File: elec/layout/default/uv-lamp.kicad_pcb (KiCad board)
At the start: 2 copper layers, 21 x 21 mm, 3 parts, among them U1 ?, U2 ?, U3 ?

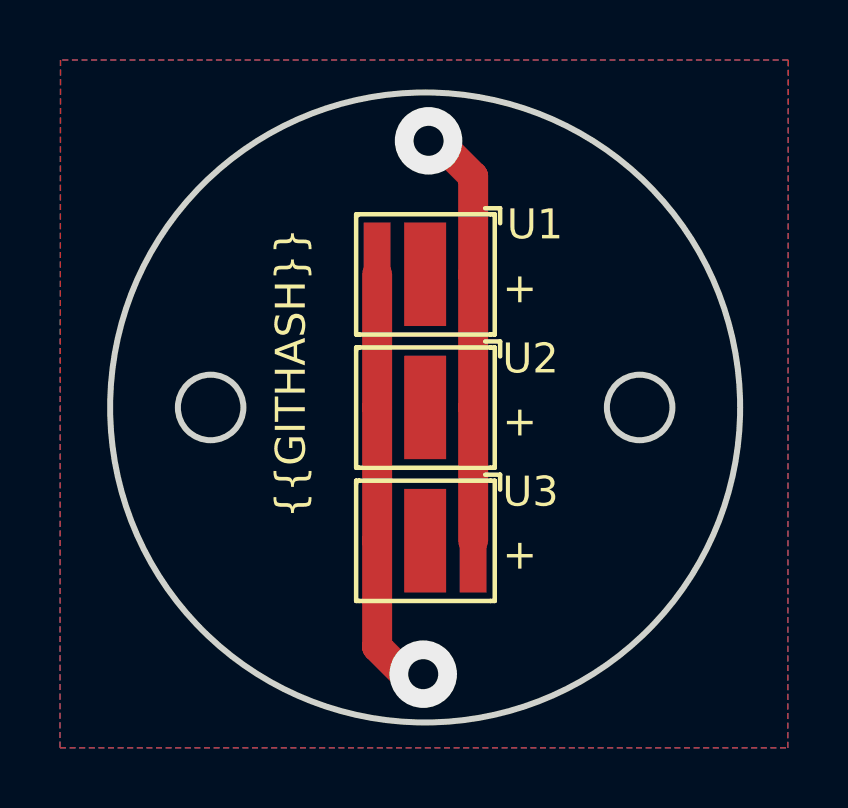
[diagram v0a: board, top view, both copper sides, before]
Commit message: removed uv-lamp build PCB bottom layer
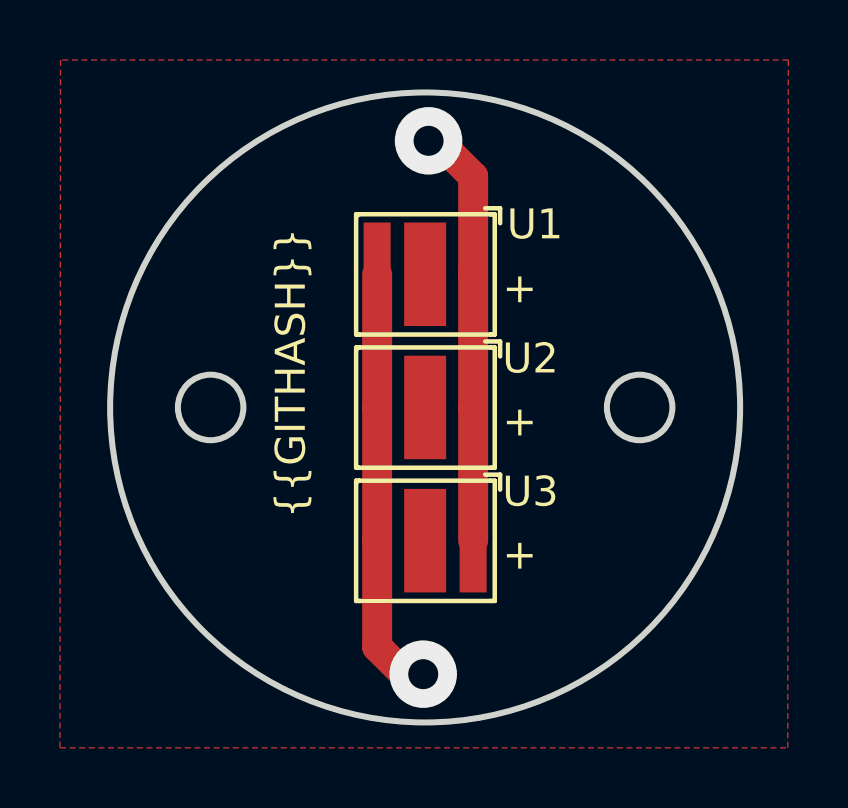
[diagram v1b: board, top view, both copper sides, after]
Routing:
- removed copper zone on B.Cu, net (none)
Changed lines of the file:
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@@
+	)
+	(zone
+		(net 0)
+		(net_name "")
+		(layer "F.Cu")
+		(hatch edge 0.5)
+		(priority 1)
+		(connect_pads
+			(clearance 0.5)
+		)
+		(min_thickness 0.25)
+		(filled_areas_thickness no)
+		(fill yes
+			(thermal_gap 0.7)
+			(thermal_bridge_width 0.5)
+			(island_removal_mode 1)
+			(island_area_min 10)
+		)
+		(polygon
+			(pts
+				(xy 159.995473 74.727755) (xy 135.735473 74.727755) (xy 135.718641 97.655363) (xy 159.978641 97.655363)
+			)
+		)
 	)
 	(zone
@@
 			)
 		)
-	)
-	(zone
-		(net 0)
-		(net_name "")
-		(layers "F&B.Cu")
-		(hatch edge 0.5)
-		(priority 1)
-		(connect_pads
-			(clearance 0.5)
-		)
-		(min_thickness 0.25)
-		(filled_areas_thickness no)
-		(fill yes
-			(thermal_gap 0.7)
-			(thermal_bridge_width 0.5)
-			(island_removal_mode 1)
-			(island_area_min 10)
-		)
-		(polygon
-			(pts
-				(xy 159.995473 74.727755) (xy 135.735473 74.727755) (xy 135.718641 97.655363) (xy 159.978641 97.655363)
-			)
-		)

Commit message: readme
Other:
- outline, holes or cut-outs redrawn
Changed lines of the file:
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@@
 	(gr_circle
 		(center 155.04 86.31)
-		(end 156.132 86.31)
+		(end 156.14 86.31)
 		(stroke
 			(width 0.2)
@@
 	(gr_circle
 		(center 140.74 86.31)
-		(end 141.832 86.31)
+		(end 141.84 86.31)
 		(stroke
 			(width 0.2)

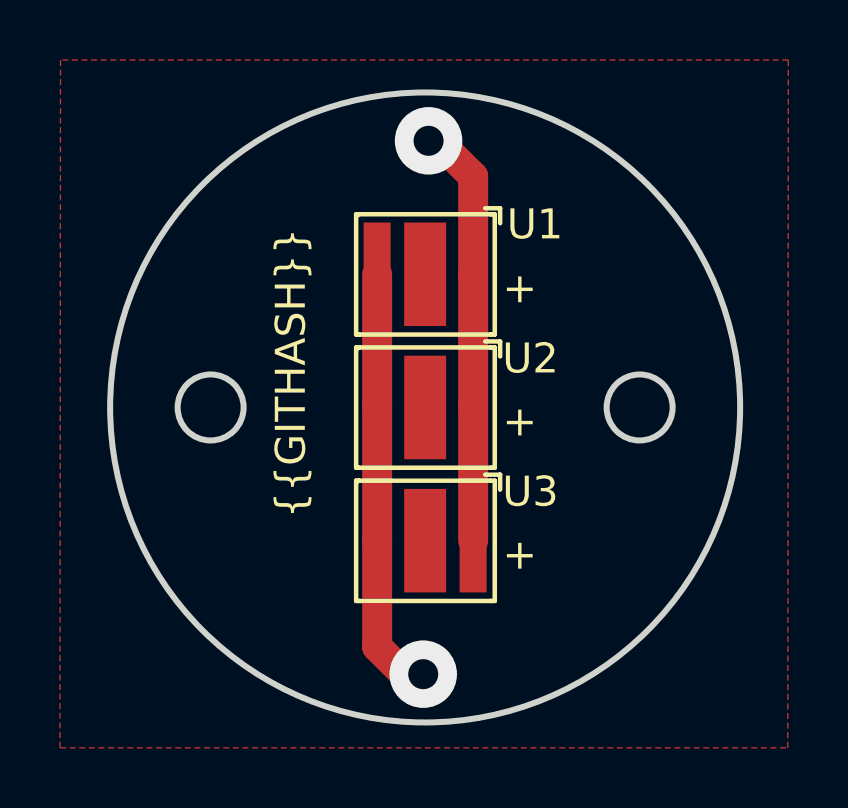
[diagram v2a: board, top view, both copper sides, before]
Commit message: added bms
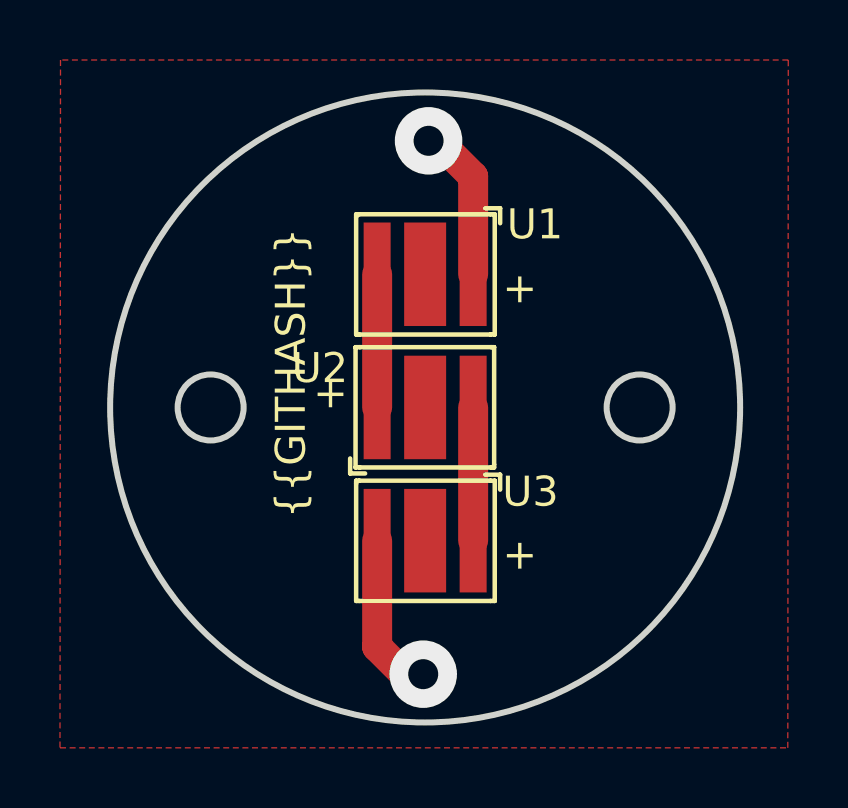
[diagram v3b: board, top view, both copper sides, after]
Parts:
- turned U2 to 180 degrees
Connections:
- U1 pad 1: k -> led1-k
- U1 pad 2: a -> vcc
- U2 pad 1: k -> led2-k
- U2 pad 2: a -> led1-k
- U3 pad 1: k -> gnd
- U3 pad 2: a -> led2-k
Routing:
- net k: track 14.5 -> 0.00 mm, vias 1 -> 0
- net a: track 14.2 -> 0.00 mm, vias 1 -> 0
- net gnd: track 0.00 -> 5.58 mm, vias 0 -> 1
- net vcc: track 0.00 -> 5.36 mm, vias 0 -> 1
- net led2-k: track 0.00 -> 4.44 mm
- net led1-k: track 0.00 -> 4.44 mm
